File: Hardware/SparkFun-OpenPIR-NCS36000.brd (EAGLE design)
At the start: 27.9 x 35.6 mm, 33 parts, among them U1 NCS36000, U2 PIR

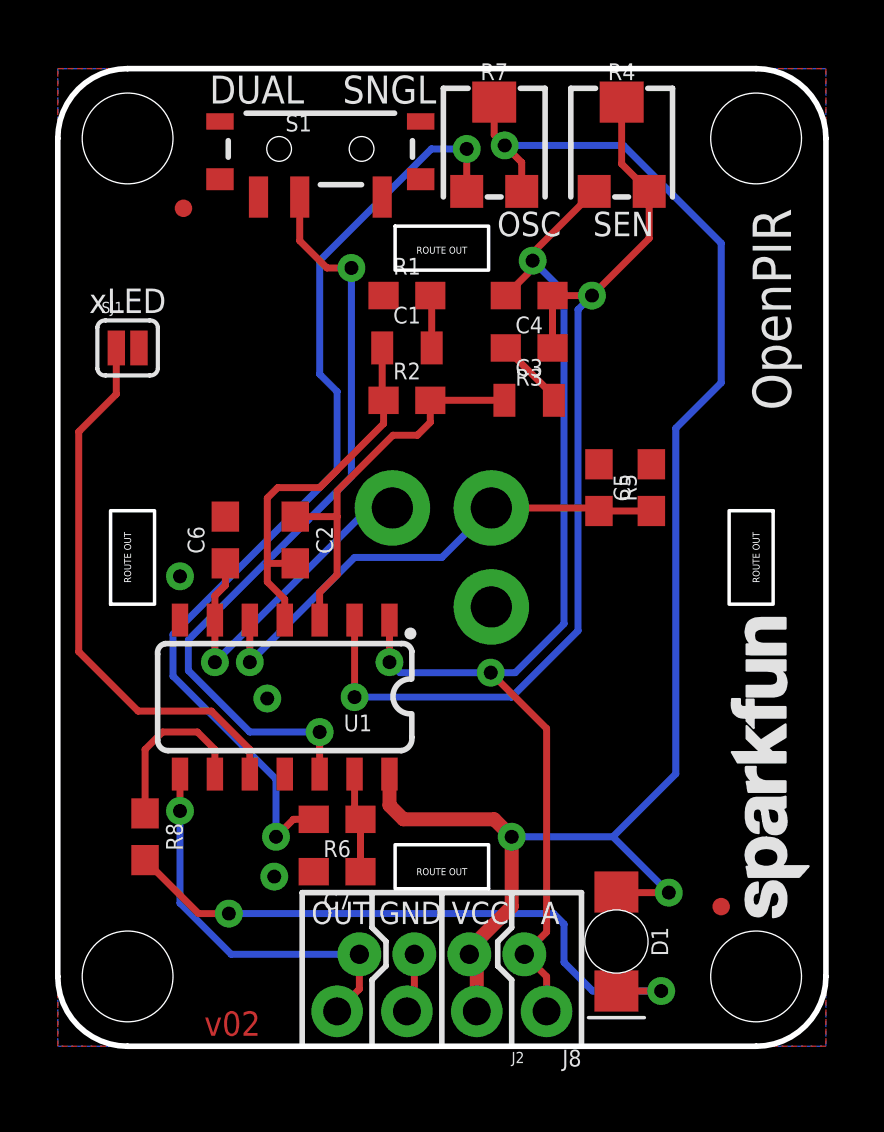
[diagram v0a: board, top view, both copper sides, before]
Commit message: Adding test points to trimpot wipers
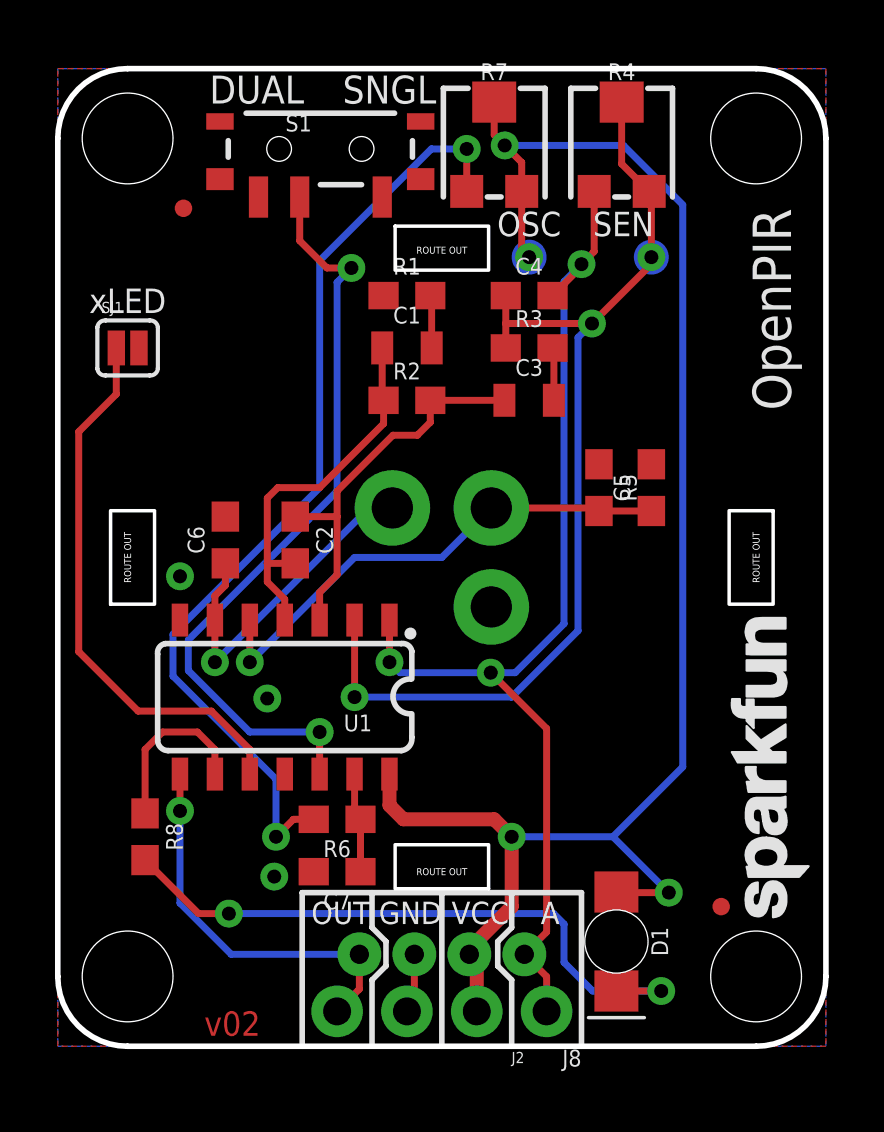
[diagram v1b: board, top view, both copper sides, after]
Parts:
- added TP1, TP2: (no value), SparkFun-Connectors:PAD.03X.05
- turned C4 to 0 degrees
- turned R3 to 0 degrees
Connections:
- net N$7: now also TP1.P$1
- net VCC: now also TP2.P$1
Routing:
- net N$7: track 36.0 -> 37.8 mm, vias 2 -> 3
- net VCC: track 57.9 -> 59.6 mm, vias 3 -> 4
- net A_OUT: track 41.7 -> 40.6 mm
- net N$4: track 2.63 -> 1.93 mm
- net N$11: track 35.5 -> 34.9 mm
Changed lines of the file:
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@@
 <attribute name="PROD_ID" value="CAP-08402" x="17.145" y="23.495" size="1.778" layer="27" display="off"/>
 </element>
-<element name="R3" library="SparkFun-Resistors" package="0603" value="10k" x="17.145" y="25.4" rot="R180">
-<attribute name="PROD_ID" value="RES-00824" x="17.145" y="25.4" size="1.778" layer="27" font="vector" ratio="15" rot="R180" display="off"/>
-</element>
-<element name="C4" library="SparkFun-Capacitors" package="0603" value="10nF" x="17.145" y="27.305" rot="R180">
-<attribute name="PROD_ID" value="CAP-00867" x="17.145" y="27.305" size="1.778" layer="27" font="vector" ratio="15" rot="R180" display="off"/>
+<element name="R3" library="SparkFun-Resistors" package="0603" value="10k" x="17.145" y="25.4">
+<attribute name="PROD_ID" value="RES-00824" x="17.145" y="25.4" size="1.778" layer="27" font="vector" ratio="15" display="off"/>
+</element>
+<element name="C4" library="SparkFun-Capacitors" package="0603" value="10nF" x="17.145" y="27.305">
+<attribute name="PROD_ID" value="CAP-00867" x="17.145" y="27.305" size="1.778" layer="27" font="vector" ratio="15" display="off"/>
 </element>
 <element name="R4" library="openPIR-temp" package="TRIMPOT-TC33X" value="1M" x="20.5105" y="32.893">
@@
 <element name="FD1" library="SparkFun-Aesthetics" package="MICRO-FIDUCIAL" value="FIDUCIALUFIDUCIAL" x="4.572" y="30.48"/>
 <element name="FD2" library="SparkFun-Aesthetics" package="MICRO-FIDUCIAL" value="FIDUCIALUFIDUCIAL" x="24.13" y="5.08"/>
+<element name="TP1" library="SparkFun-Connectors" package="PAD.03X.05" value="" x="21.59" y="28.702" rot="MR0"/>
+<element name="TP2" library="SparkFun-Connectors" package="PAD.03X.05" value="" x="17.145" y="28.702" rot="MR0"/>
 </elements>
 <signals>
@@
 <wire x1="12.065" y1="8.763" x2="12.573" y2="8.255" width="0.508" layer="1"/>
 <via x="16.51" y="7.62" extent="1-16" drill="0.508"/>
-<wire x1="22.479" y1="22.479" x2="24.13" y2="24.13" width="0.254" layer="16"/>
-<wire x1="24.13" y1="24.13" x2="24.13" y2="29.21" width="0.254" layer="16"/>
 <via x="16.256" y="32.766" extent="1-16" drill="0.508"/>
-<wire x1="24.13" y1="29.21" x2="20.574" y2="32.766" width="0.254" layer="16"/>
 <wire x1="20.574" y1="32.766" x2="16.256" y2="32.766" width="0.254" layer="16"/>
 <wire x1="15.875" y1="34.343" x2="15.875" y2="33.147" width="0.254" layer="1"/>
@@
 <wire x1="22.225" y1="5.588" x2="20.193" y2="7.62" width="0.254" layer="16"/>
 <wire x1="20.193" y1="7.62" x2="16.51" y2="7.62" width="0.254" layer="16"/>
-<wire x1="20.193" y1="7.62" x2="22.479" y2="9.906" width="0.254" layer="16"/>
-<wire x1="22.479" y1="9.906" x2="22.479" y2="22.479" width="0.254" layer="16"/>
+<wire x1="20.193" y1="7.62" x2="22.733" y2="10.16" width="0.254" layer="16"/>
+<wire x1="22.733" y1="10.16" x2="22.733" y2="30.607" width="0.254" layer="16"/>
+<contactref element="TP2" pad="P$1"/>
+<via x="17.145" y="28.702" extent="1-16" drill="0.508"/>
+<wire x1="16.875" y1="28.972" x2="17.145" y2="28.702" width="0.254" layer="16"/>
+<wire x1="22.733" y1="30.607" x2="20.574" y2="32.766" width="0.254" layer="16"/>
+<wire x1="16.875" y1="31.093" x2="16.875" y2="28.972" width="0.254" layer="1"/>
+<wire x1="16.875" y1="28.972" x2="17.145" y2="28.702" width="0.254" layer="1"/>
 </signal>
 <signal name="N$3">
@@
 <contactref element="C3" pad="2"/>
 <contactref element="R3" pad="2"/>
-<wire x1="16.295" y1="25.4" x2="18.045" y2="23.65" width="0.254" layer="1"/>
-<wire x1="18.045" y1="23.65" x2="18.045" y2="23.495" width="0.254" layer="1"/>
+<wire x1="18.045" y1="23.495" x2="18.045" y2="25.35" width="0.254" layer="1"/>
+<wire x1="18.045" y1="25.35" x2="17.995" y2="25.4" width="0.254" layer="1"/>
 </signal>
 <signal name="N$5">
@@
 <contactref element="R4" pad="3"/>
 <wire x1="20.5105" y1="32.093" x2="21.5105" y2="31.093" width="0.254" layer="1"/>
-<wire x1="17.995" y1="27.305" x2="17.995" y2="25.4" width="0.254" layer="1"/>
 <wire x1="10.795" y1="12.7" x2="16.51" y2="12.7" width="0.254" layer="16"/>
 <wire x1="16.51" y1="12.7" x2="18.923" y2="15.113" width="0.254" layer="16"/>
-<wire x1="18.923" y1="15.113" x2="18.923" y2="26.797" width="0.254" layer="16"/>
-<wire x1="18.923" y1="26.797" x2="19.431" y2="27.305" width="0.254" layer="16"/>
-<via x="19.431" y="27.305" extent="1-16" drill="0.508"/>
-<wire x1="19.431" y1="27.305" x2="17.995" y2="27.305" width="0.254" layer="1"/>
-<wire x1="19.431" y1="27.305" x2="21.5105" y2="29.3845" width="0.254" layer="1"/>
-<wire x1="21.5105" y1="29.3845" x2="21.5105" y2="31.093" width="0.254" layer="1"/>
+<wire x1="18.923" y1="15.113" x2="18.923" y2="25.781" width="0.254" layer="16"/>
+<wire x1="18.923" y1="25.781" x2="19.431" y2="26.289" width="0.254" layer="16"/>
+<via x="19.431" y="26.289" extent="1-16" drill="0.508"/>
+<contactref element="TP1" pad="P$1"/>
+<wire x1="16.295" y1="25.4" x2="16.295" y2="26.289" width="0.254" layer="1"/>
+<wire x1="16.295" y1="26.289" x2="16.295" y2="27.305" width="0.254" layer="1"/>
+<wire x1="19.431" y1="26.289" x2="16.295" y2="26.289" width="0.254" layer="1"/>
+<via x="21.59" y="28.702" extent="1-16" drill="0.508"/>
+<wire x1="19.431" y1="26.289" x2="21.59" y2="28.448" width="0.254" layer="1"/>
+<wire x1="21.59" y1="28.448" x2="21.59" y2="28.702" width="0.254" layer="1"/>
+<wire x1="21.59" y1="28.702" x2="21.59" y2="31.0135" width="0.254" layer="1"/>
+<wire x1="21.59" y1="31.0135" x2="21.5105" y2="31.093" width="0.254" layer="1"/>
 </signal>
 <signal name="N$8">
@@
 <wire x1="9.525" y1="11.43" x2="6.985" y2="11.43" width="0.254" layer="16"/>
 <wire x1="4.7498" y1="13.6652" x2="4.7498" y2="14.7828" width="0.254" layer="16"/>
-<wire x1="4.7498" y1="14.7828" x2="10.68" y2="20.713" width="0.254" layer="16"/>
 <wire x1="6.985" y1="11.43" x2="4.7498" y2="13.6652" width="0.254" layer="16"/>
-<wire x1="10.68" y1="20.713" x2="10.68" y2="28.309" width="0.254" layer="16"/>
 <via x="10.68" y="28.309" extent="1-16" drill="0.508"/>
 <wire x1="8.8004" y1="29.2996" x2="8.8004" y2="30.889" width="0.254" layer="1"/>
 <wire x1="10.68" y1="28.309" x2="9.791" y2="28.309" width="0.254" layer="1"/>
 <wire x1="9.791" y1="28.309" x2="8.8004" y2="29.2996" width="0.254" layer="1"/>
+<wire x1="4.7498" y1="14.7828" x2="10.16" y2="20.193" width="0.254" layer="16"/>
+<wire x1="10.16" y1="20.193" x2="10.16" y2="27.789" width="0.254" layer="16"/>
+<wire x1="10.16" y1="27.789" x2="10.68" y2="28.309" width="0.254" layer="16"/>
 </signal>
 <signal name="!LED_EN!">
@@
 <wire x1="7.9375" y1="9.7155" x2="4.191" y2="13.462" width="0.254" layer="16"/>
 <wire x1="4.191" y1="13.462" x2="4.191" y2="14.986" width="0.254" layer="16"/>
-<wire x1="4.191" y1="14.986" x2="10.16" y2="20.955" width="0.254" layer="16"/>
-<wire x1="10.16" y1="20.955" x2="10.16" y2="23.8125" width="0.254" layer="16"/>
-<wire x1="10.16" y1="23.8125" x2="9.525" y2="24.4475" width="0.254" layer="16"/>
 <wire x1="14.875" y1="31.093" x2="14.875" y2="32.639" width="0.254" layer="1"/>
 <via x="14.875" y="32.639" extent="1-16" drill="0.508"/>
 <wire x1="14.875" y1="32.639" x2="13.589" y2="32.639" width="0.254" layer="16"/>
 <wire x1="9.525" y1="28.575" x2="13.589" y2="32.639" width="0.254" layer="16"/>
-<wire x1="9.525" y1="24.4475" x2="9.525" y2="28.575" width="0.254" layer="16"/>
+<wire x1="4.191" y1="14.986" x2="9.525" y2="20.32" width="0.254" layer="16"/>
+<wire x1="9.525" y1="20.32" x2="9.525" y2="28.575" width="0.254" layer="16"/>
 </signal>
 <signal name="A_OUT">
@@
 <wire x1="12.065" y1="15.5" x2="12.065" y2="13.97" width="0.254" layer="1"/>
 <via x="12.065" y="13.97" extent="1-16" drill="0.508"/>
-<wire x1="18.415" y1="15.367" x2="18.415" y2="27.432" width="0.254" layer="16"/>
+<wire x1="18.415" y1="15.367" x2="18.415" y2="27.813" width="0.254" layer="16"/>
 <contactref element="J2" pad="1"/>
 <via x="15.748" y="13.589" extent="1-16" drill="0.508"/>
@@
 <wire x1="15.748" y1="13.589" x2="16.637" y2="13.589" width="0.254" layer="16"/>
 <wire x1="16.637" y1="13.589" x2="18.415" y2="15.367" width="0.254" layer="16"/>
-<wire x1="18.415" y1="27.432" x2="17.272" y2="28.575" width="0.254" layer="16"/>
-<via x="17.272" y="28.575" extent="1-16" drill="0.508"/>
-<wire x1="17.272" y1="28.575" x2="17.272" y2="28.282" width="0.254" layer="1"/>
-<wire x1="17.272" y1="28.282" x2="16.295" y2="27.305" width="0.254" layer="1"/>
 <wire x1="17.78" y1="11.557" x2="15.748" y2="13.589" width="0.254" layer="1"/>
-<wire x1="17.272" y1="28.575" x2="17.272" y2="28.8545" width="0.254" layer="1"/>
-<wire x1="17.272" y1="28.8545" x2="19.5105" y2="31.093" width="0.254" layer="1"/>
+<wire x1="18.415" y1="27.813" x2="19.05" y2="28.448" width="0.254" layer="16"/>
+<via x="19.05" y="28.448" extent="1-16" drill="0.508"/>
+<wire x1="19.05" y1="28.448" x2="19.05" y2="28.36" width="0.254" layer="1"/>
+<wire x1="19.05" y1="28.36" x2="17.995" y2="27.305" width="0.254" layer="1"/>
+<wire x1="19.05" y1="28.448" x2="19.5105" y2="28.9085" width="0.254" layer="1"/>
+<wire x1="19.5105" y1="28.9085" x2="19.5105" y2="31.093" width="0.254" layer="1"/>
 </signal>
 </signals>

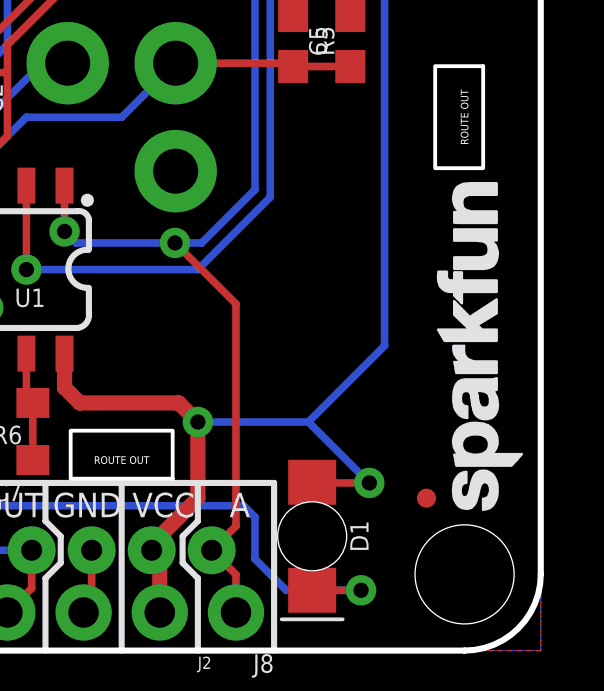
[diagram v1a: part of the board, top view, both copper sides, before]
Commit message: Replacing text logo with text+flame, moving schematic fids.
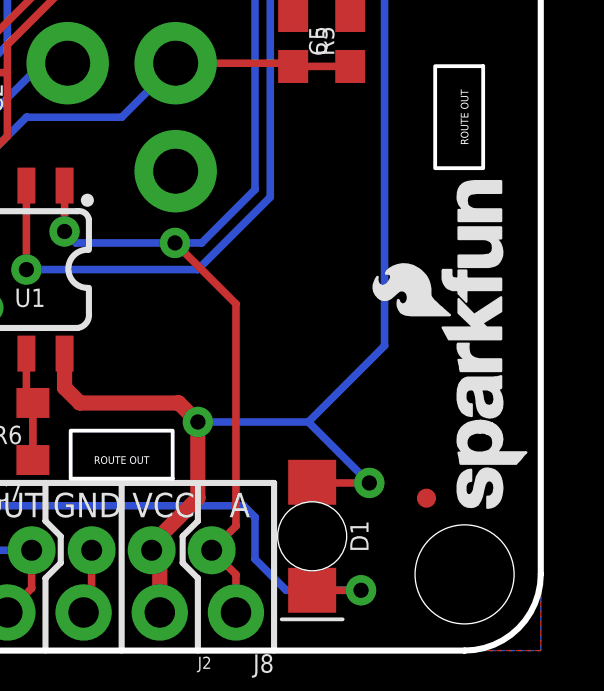
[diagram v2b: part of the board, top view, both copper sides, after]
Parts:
- LOGO1: value SFE_LOGO_NAME.1_INCH -> SFE_LOGO_NAME_FLAME.1_INCH; device SparkFun-Aesthetics:SFE_LOGO_NAME_.1 -> SparkFun-Aesthetics:SFE_LOGO_NAME_FLAME_.1
- moved LOGO1 0.28 mm to (27.6, 4.32)
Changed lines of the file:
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@@
 <attribute name="PROD_ID" value="RES-08495" x="10.16" y="8.255" size="1.778" layer="27" rot="R180" display="off"/>
 </element>
-<element name="LOGO1" library="SparkFun-Aesthetics" package="SFE_LOGO_NAME_.1" value="SFE_LOGO_NAME.1_INCH" x="27.813" y="4.191" rot="R90"/>
+<element name="LOGO1" library="SparkFun-Aesthetics" package="SFE_LOGO_NAME_FLAME_.1" value="SFE_LOGO_NAME_FLAME.1_INCH" x="27.559" y="4.318" rot="R90"/>
 <element name="LOGO3" library="SparkFun-Aesthetics" package="SFE_LOGO_NAME_.1" value="SFE_LOGO_NAME.1_INCH" x="22.987" y="31.877" rot="MR0"/>
 <element name="LOGO4" library="SparkFun-Aesthetics" package="OSHW-LOGO-S" value="OSHW-LOGOS" x="5.969" y="33.528" rot="MR0"/>
